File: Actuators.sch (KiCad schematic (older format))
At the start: 14 parts, among them J1 SERVO DCDC 5V, J3 Actuator1, J4 Actuator2, M1 Motor_Servo, M2 Motor_Servo, U6 DRV8847_TSSOP

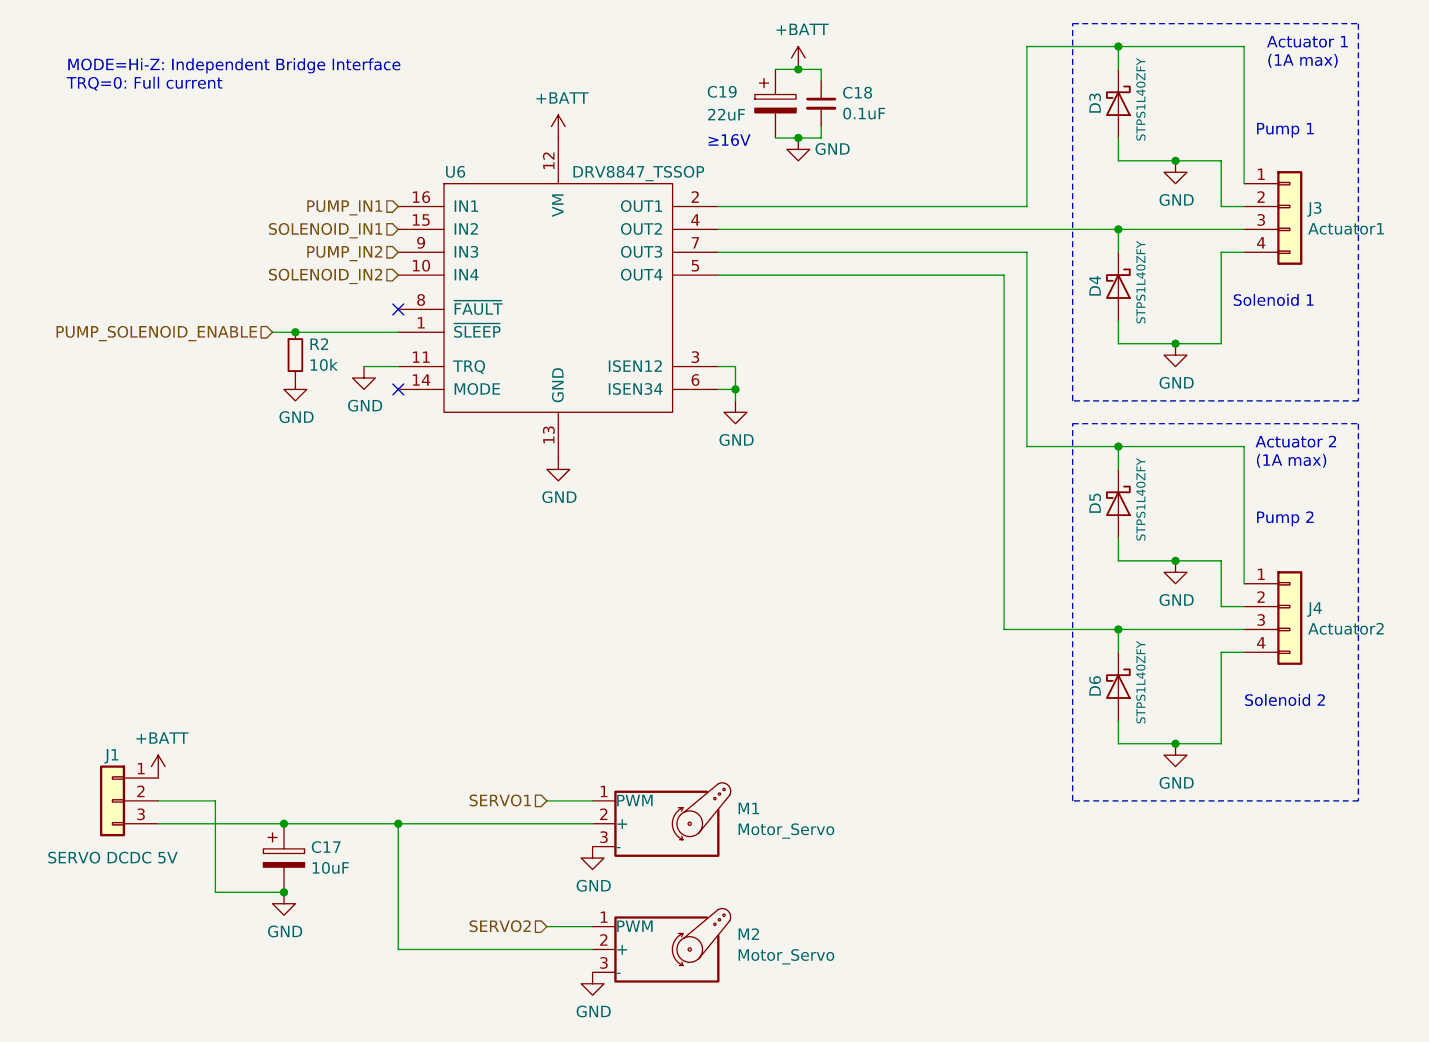
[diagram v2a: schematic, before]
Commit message: Update footprints, better refdes, cleanup schematic, 40x22mm outline
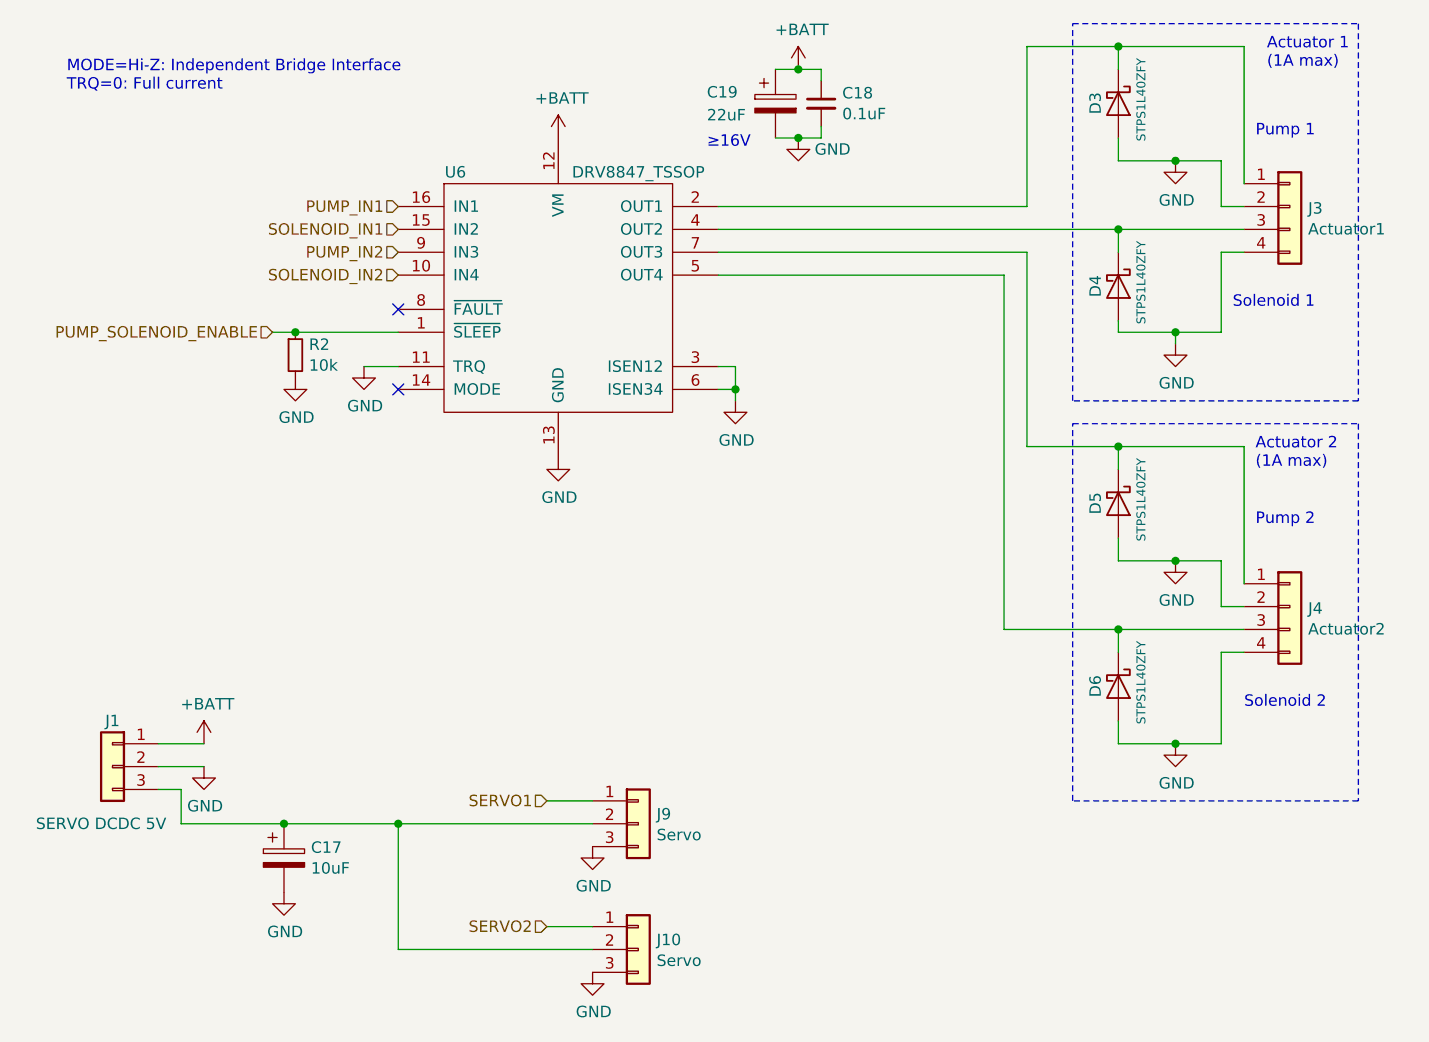
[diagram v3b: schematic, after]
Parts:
- removed M1, M2: Motor_Servo, Connector_Molex:Molex_PicoBlade_53261-0371_1x03-1MP_P1.25mm_Horizontal, symbol Motor:Motor_Servo
- added J10, J9: Servo, Connector_Molex:Molex_PicoBlade_53261-0371_1x03-1MP_P1.25mm_Horizontal, symbol Connector_Generic:Conn_01x03
- C19: footprint Capacitor_SMD:CP_Elec_5x5.8 -> Capacitor_SMD:C_1206_3216Metric
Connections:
- net GND: now also J10.3 (Pin_3), J9.3 (Pin_3)
- net SERVO1: now also J9.1 (Pin_1)
- net SERVO2: now also J10.1 (Pin_1)
- net at C17.1, J1.3 (Pin_3): now also J10.2 (Pin_2), J9.2 (Pin_2)
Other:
- moved on the sheet: J1
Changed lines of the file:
@@
 EESchema Schematic File Version 4
+LIBS:actuator-board-cache
 EELAYER 30 0
 EELAYER END
@@
 L Connector_Generic:Conn_01x03 J1
 U 1 1 5E3C2833
-P 2600 5250
-F 0 "J1" H 2600 5450 50  0000 C CNN
-F 1 "SERVO DCDC 5V" H 2600 5000 50  0000 C CNN
-F 2 "Connector_PinHeader_2.54mm:PinHeader_1x03_P2.54mm_Vertical" H 2600 5250 50  0001 C CNN
-F 3 "~" H 2600 5250 50  0001 C CNN
-F 4 "1" H 2600 5250 50  0001 C CNN "DNP"
-	1    2600 5250
+P 2600 5100
+F 0 "J1" H 2600 5300 50  0000 C CNN
+F 1 "SERVO DCDC 5V" H 2650 4850 50  0000 C CNN
+F 2 "Connector_PinHeader_2.54mm:PinHeader_1x03_P2.54mm_Vertical" H 2600 5100 50  0001 C CNN
+F 3 "~" H 2600 5100 50  0001 C CNN
+F 4 "1" H 2600 5100 50  0001 C CNN "DNP"
+	1    2600 5100
 	-1   0    0    -1
 $EndComp
 Wire Wire Line
-	2800 5250 3050 5250
-Wire Wire Line
-	3050 5250 3050 5650
-Wire Wire Line
-	3050 5650 3350 5650
-Wire Wire Line
-	2800 5350 3350 5350
-Connection ~ 3350 5350
-Wire Wire Line
 	3350 5350 3850 5350
-Connection ~ 3350 5650
 Wire Wire Line
 	3850 5350 3850 5900
@@
 $EndComp
 Wire Wire Line
-	7000 3150 7000 3250
-Wire Wire Line
 	5250 2750 7000 2750
 Connection ~ 7000 2750
@@
 Wire Wire Line
 	7250 2450 7450 2450
-Wire Wire Line
-	7000 3250 7250 3250
 $Comp
 L power:GND #PWR0103
@@
 	1    0    0    -1
 $EndComp
-Connection ~ 7250 3250
-Wire Wire Line
-	7250 3250 7450 3250
+Wire Wire Line
+	7250 3200 7450 3200
 $Comp
 L power:GND #PWR0104
@@
 F 0 "C19" H 5200 2250 50  0000 L CNN
 F 1 "22uF" H 5200 2150 50  0000 L CNN
-F 2 "Capacitor_SMD:CP_Elec_5x5.8" H 5538 2050 50  0001 C CNN
+F 2 "Capacitor_SMD:C_1206_3216Metric" H 5538 2050 50  0001 C CNN
 F 3 "~" H 5500 2200 50  0001 C CNN
 F 4 "PCE4240CT-ND" H 5500 2200 50  0001 C CNN "digikey#"
@@
 ≥16V
 $Comp
-L Motor:Motor_Servo M2
-U 1 1 5E38464C
-P 5000 5900
-F 0 "M2" H 5332 5965 50  0000 L CNN
-F 1 "Motor_Servo" H 5332 5874 50  0000 L CNN
-F 2 "Connector_Molex:Molex_PicoBlade_53261-0371_1x03-1MP_P1.25mm_Horizontal" H 5000 5710 50  0001 C CNN
-F 3 "http://forums.parallax.com/uploads/attachments/46831/74481.png" H 5000 5710 50  0001 C CNN
-	1    5000 5900
-	1    0    0    -1
-$EndComp
-$Comp
-L Motor:Motor_Servo M1
-U 1 1 5E37BD0B
-P 5000 5350
-F 0 "M1" H 5332 5415 50  0000 L CNN
-F 1 "Motor_Servo" H 5332 5324 50  0000 L CNN
-F 2 "Connector_Molex:Molex_PicoBlade_53261-0371_1x03-1MP_P1.25mm_Horizontal" H 5000 5160 50  0001 C CNN
-F 3 "http://forums.parallax.com/uploads/attachments/46831/74481.png" H 5000 5160 50  0001 C CNN
-F 4 "WM7621CT-ND" H 5000 5350 50  0001 C CNN "digikey#"
-	1    5000 5350
-	1    0    0    -1
-$EndComp
-$Comp
 L Connector_Generic:Conn_01x04 J3
 U 1 1 5E485C32
@@
 	7550 2850 7450 2850
 Wire Wire Line
-	7450 2850 7450 3250
+	7450 2850 7450 3200
 Wire Wire Line
 	7000 4500 7550 4500
@@
 L power:+BATT #PWR0111
 U 1 1 5E4B1181
-P 2800 5150
-F 0 "#PWR0111" H 2800 5000 50  0001 C CNN
-F 1 "+BATT" H 2815 5323 50  0000 C CNN
-F 2 "" H 2800 5150 50  0001 C CNN
-F 3 "" H 2800 5150 50  0001 C CNN
-	1    2800 5150
-	1    0    0    -1
-$EndComp
+P 3000 5000
+F 0 "#PWR0111" H 3000 4850 50  0001 C CNN
+F 1 "+BATT" H 3015 5173 50  0000 C CNN
+F 2 "" H 3000 5000 50  0001 C CNN
+F 3 "" H 3000 5000 50  0001 C CNN
+	1    3000 5000
+	1    0    0    -1
+$EndComp
+Wire Wire Line
+	7250 3250 7250 3200
+$Comp
+L power:GND #PWR?
+U 1 1 5E4BE752
+P 3000 5100
+AR Path="/5E4BE752" Ref="#PWR?"  Part="1"
+AR Path="/5E1FB153/5E4BE752" Ref="#PWR0112"  Part="1"
+F 0 "#PWR0112" H 3000 4850 50  0001 C CNN
+F 1 "GND" H 3005 4927 50  0000 C CNN
+F 2 "" H 3000 5100 50  0001 C CNN
+F 3 "" H 3000 5100 50  0001 C CNN
+	1    3000 5100
+	1    0    0    -1
+$EndComp
+Wire Wire Line
+	2800 5100 3000 5100
+Wire Wire Line
+	3000 5000 2800 5000
+Connection ~ 3350 5350
+Wire Wire Line
+	2900 5200 2900 5350
+Wire Wire Line
+	2800 5200 2900 5200
+Wire Wire Line
+	2900 5350 3350 5350
+Wire Wire Line
+	7000 3150 7000 3200
+Wire Wire Line
+	7000 3200 7250 3200
+Connection ~ 7250 3200
+$Comp
+L Connector_Generic:Conn_01x03 J9
+U 1 1 5E4FD67B
+P 4900 5350
+F 0 "J9" H 4980 5392 50  0000 L CNN
+F 1 "Servo" H 4980 5301 50  0000 L CNN
+F 2 "Connector_Molex:Molex_PicoBlade_53261-0371_1x03-1MP_P1.25mm_Horizontal" H 4900 5350 50  0001 C CNN
+F 3 "~" H 4900 5350 50  0001 C CNN
+F 4 "WM7621CT-ND" H 4900 5350 50  0001 C CNN "digikey#"
+	1    4900 5350
+	1    0    0    -1
+$EndComp
+$Comp
+L Connector_Generic:Conn_01x03 J10
+U 1 1 5E50039E
+P 4900 5900
+F 0 "J10" H 4980 5942 50  0000 L CNN
+F 1 "Servo" H 4980 5851 50  0000 L CNN
+F 2 "Connector_Molex:Molex_PicoBlade_53261-0371_1x03-1MP_P1.25mm_Horizontal" H 4900 5900 50  0001 C CNN
+F 3 "~" H 4900 5900 50  0001 C CNN
+F 4 "WM7621CT-ND" H 4900 5900 50  0001 C CNN "digikey#"
+	1    4900 5900
+	1    0    0    -1
+$EndComp

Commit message: HTSSOP motor driver, component arrangment, added MCU capacitor
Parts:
- C17, C19: symbol Device:CP -> Device:C_Small
- U6: footprint Package_SO:TSSOP-16_4.4x5mm_P0.65mm -> Package_SO:TSSOP-16-1EP_4.4x5mm_P0.65mm; symbol _power:DRV8847_TSSOP -> _power:DRV8847_HTSSOP; digikey# 296-53425-1-ND -> (none)
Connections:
- net GND: now also U6.17 (PAD)
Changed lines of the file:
@@
 SOLENOID_IN1
 $Comp
-L Device:CP C?
+L Device:C_Small C?
 U 1 1 5E3A79F5
-P 3350 5500
+P 3350 5450
 AR Path="/5E3A79F5" Ref="C?"  Part="1"
 AR Path="/5E1FB153/5E3A79F5" Ref="C17"  Part="1"
-F 0 "C17" H 3468 5546 50  0000 L CNN
-F 1 "10uF" H 3468 5455 50  0000 L CNN
-F 2 "Capacitor_SMD:C_1206_3216Metric" H 3388 5350 50  0001 C CNN
-F 3 "~" H 3350 5500 50  0001 C CNN
-F 4 "399-7442-1-ND" H 3350 5500 50  0001 C CNN "digikey#"
-	1    3350 5500
+F 0 "C17" H 3468 5496 50  0000 L CNN
+F 1 "10uF" H 3468 5405 50  0000 L CNN
+F 2 "Capacitor_SMD:C_1206_3216Metric" H 3388 5300 50  0001 C CNN
+F 3 "~" H 3350 5450 50  0001 C CNN
+F 4 "399-7442-1-ND" H 3350 5450 50  0001 C CNN "digikey#"
+	1    3350 5450
 	1    0    0    -1
 $EndComp
@@
 L power:GND #PWR?
 U 1 1 5E3A79FB
-P 3350 5650
+P 3350 5550
 AR Path="/5E3A79FB" Ref="#PWR?"  Part="1"
 AR Path="/5E1FB153/5E3A79FB" Ref="#PWR035"  Part="1"
-F 0 "#PWR035" H 3350 5400 50  0001 C CNN
-F 1 "GND" H 3355 5477 50  0000 C CNN
-F 2 "" H 3350 5650 50  0001 C CNN
-F 3 "" H 3350 5650 50  0001 C CNN
-	1    3350 5650
+F 0 "#PWR035" H 3350 5300 50  0001 C CNN
+F 1 "GND" H 3355 5377 50  0000 C CNN
+F 2 "" H 3350 5550 50  0001 C CNN
+F 3 "" H 3350 5550 50  0001 C CNN
+	1    3350 5550
 	1    0    0    -1
 $EndComp
@@
 Actuator 2\n(1A max)
 $Comp
-L _power:DRV8847_TSSOP U6
+L _power:DRV8847_HTSSOP U6
 U 1 1 5E3FBC0B
 P 4550 3050
 F 0 "U6" H 4100 3600 50  0000 C CNN
 F 1 "DRV8847_TSSOP" H 4900 3600 50  0000 C CNN
-F 2 "Package_SO:TSSOP-16_4.4x5mm_P0.65mm" H 4550 3000 50  0001 C CNN
+F 2 "Package_SO:TSSOP-16-1EP_4.4x5mm_P0.65mm" H 4550 3000 50  0001 C CNN
 F 3 "http://www.ti.com/lit/ds/symlink/drv8847.pdf" H 4550 3000 50  0001 C CNN
-F 4 "296-53425-1-ND" H 4550 3050 50  0001 C CNN "digikey#"
+F 4 "" H 4550 3050 50  0001 C CNN "digikey#"
 	1    4550 3050
 	1    0    0    -1
@@
 $EndComp
 $Comp
-L Device:CP C?
+L Device:C_Small C?
 U 1 1 5E4761AC
 P 5500 2200
@@
 	1    0    0    -1
 $EndComp
+Wire Wire Line
+	5500 2100 5500 2050
+Wire Wire Line
+	5500 2300 5500 2350
+Wire Wire Line
+	4450 3750 4550 3750
+Connection ~ 4550 3750
 $EndSCHEMATC

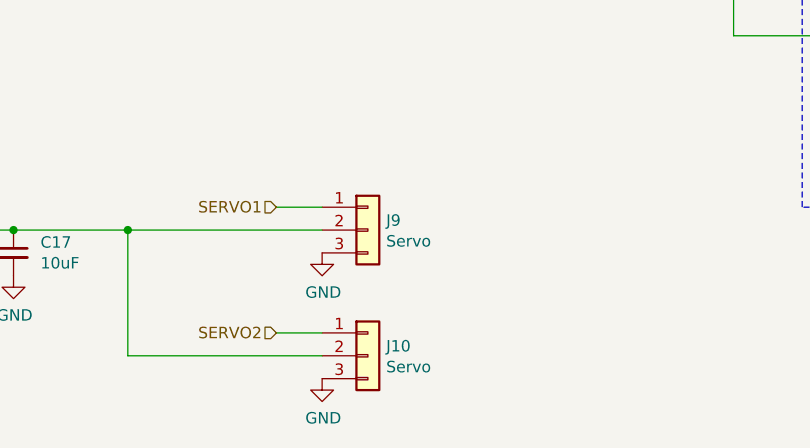
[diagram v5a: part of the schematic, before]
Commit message: Silk screen doc, ground vias, exchange servo 1 <-> 2
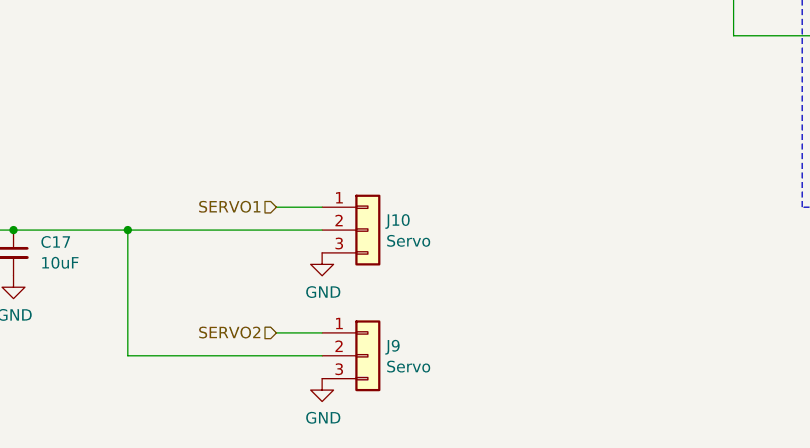
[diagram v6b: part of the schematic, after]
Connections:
- net SERVO1: now also J10.1 (Pin_1); no longer J9.1 (Pin_1)
- net SERVO2: now also J9.1 (Pin_1); no longer J10.1 (Pin_1)
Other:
- moved on the sheet: J10, J9
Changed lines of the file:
@@
 L Connector_Generic:Conn_01x03 J9
 U 1 1 5E4FD67B
+P 4900 5900
+F 0 "J9" H 4980 5942 50  0000 L CNN
+F 1 "Servo" H 4980 5851 50  0000 L CNN
+F 2 "Connector_Molex:Molex_PicoBlade_53261-0371_1x03-1MP_P1.25mm_Horizontal" H 4900 5900 50  0001 C CNN
+F 3 "~" H 4900 5900 50  0001 C CNN
+F 4 "WM7621CT-ND" H 4900 5900 50  0001 C CNN "digikey#"
+	1    4900 5900
+	1    0    0    -1
+$EndComp
+$Comp
+L Connector_Generic:Conn_01x03 J10
+U 1 1 5E50039E
 P 4900 5350
-F 0 "J9" H 4980 5392 50  0000 L CNN
+F 0 "J10" H 4980 5392 50  0000 L CNN
 F 1 "Servo" H 4980 5301 50  0000 L CNN
 F 2 "Connector_Molex:Molex_PicoBlade_53261-0371_1x03-1MP_P1.25mm_Horizontal" H 4900 5350 50  0001 C CNN
@@
 	1    0    0    -1
 $EndComp
-$Comp
-L Connector_Generic:Conn_01x03 J10
-U 1 1 5E50039E
-P 4900 5900
-F 0 "J10" H 4980 5942 50  0000 L CNN
-F 1 "Servo" H 4980 5851 50  0000 L CNN
-F 2 "Connector_Molex:Molex_PicoBlade_53261-0371_1x03-1MP_P1.25mm_Horizontal" H 4900 5900 50  0001 C CNN
-F 3 "~" H 4900 5900 50  0001 C CNN
-F 4 "WM7621CT-ND" H 4900 5900 50  0001 C CNN "digikey#"
-	1    4900 5900
-	1    0    0    -1
-$EndComp
